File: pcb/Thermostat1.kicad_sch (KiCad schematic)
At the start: 50 parts, among them J1 Screw_Terminal_01x04, J2 Conn_01x04_Female, K1 HK19F-DC_12-SHG, K2 HK19F-DC_12-SHG, Q1 SI2310B, Q2 SI2310B, SW1 SW_Push, SW2 SW_Push, SW3 SW_Push, SW4 SW_Push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

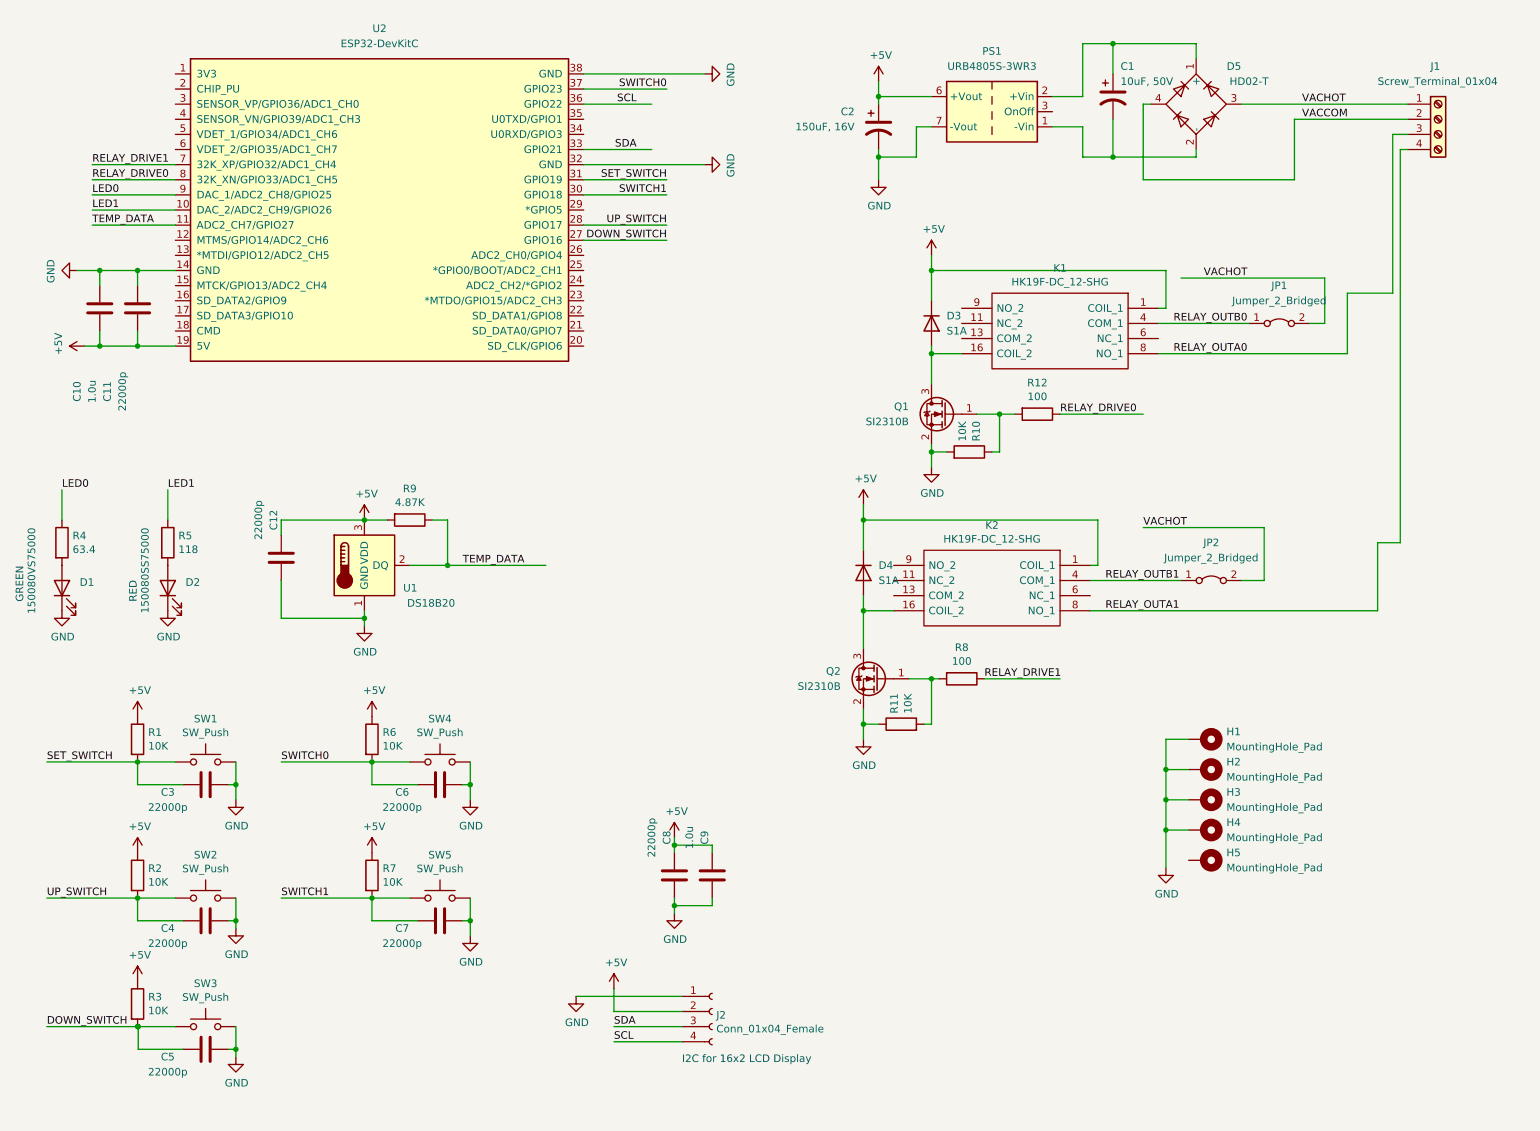
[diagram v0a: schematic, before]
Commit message: Fixed a couple issues on schematic and layout - swapped power supplies on external components and pullups from 5V to 3.3V, moved input connector so it's further from the edge of the box, increased spacing on thermometer leads to accomodate available parts and added an FCCH logo.
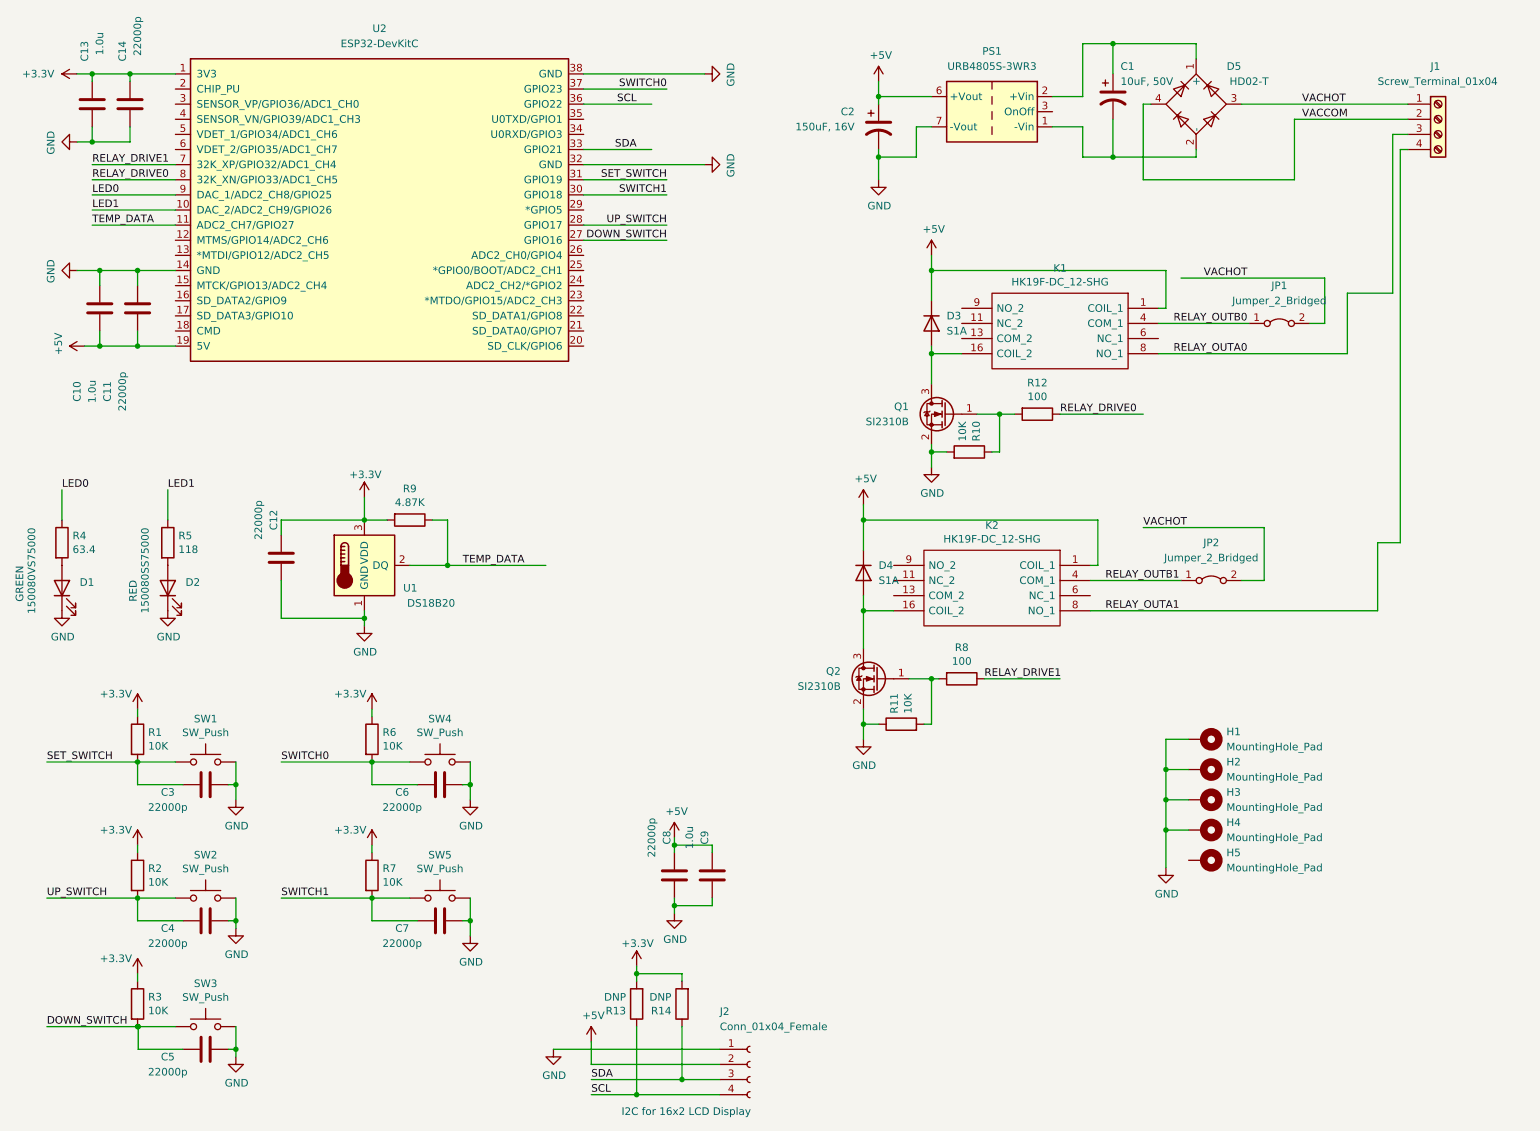
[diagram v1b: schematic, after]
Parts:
- added C13: 1.0u, Capacitor_SMD:C_0805_2012Metric_Pad1.18x1.45mm_HandSolder, symbol Device:C
- added C14: 22000p, Capacitor_SMD:C_0603_1608Metric_Pad1.08x0.95mm_HandSolder, symbol Device:C
- added R13, R14: DNP, Resistor_SMD:R_0603_1608Metric_Pad0.98x0.95mm_HandSolder, symbol Device:R
- U1: footprint Package_TO_SOT_THT:TO-92_Inline -> Package_TO_SOT_THT:TO-92_Inline_Wide
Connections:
- net +5V: no longer C12.1, R1.1, R2.1, R3.1, R6.1, R7.1, R9.2, U1.3 (VDD)
- net GND: now also C13.2, C14.2
- net SCL: now also R13.1
- net SDA: now also R14.1
- net +3.3V: now reaches U2.1 (3V3)
- net +3.3V: now also C12.1, R1.1, R2.1, R3.1, R6.1, R7.1, R9.2, U1.3 (VDD), C13.1, C14.1, R13.2, R14.2
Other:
- moved on the sheet: J2

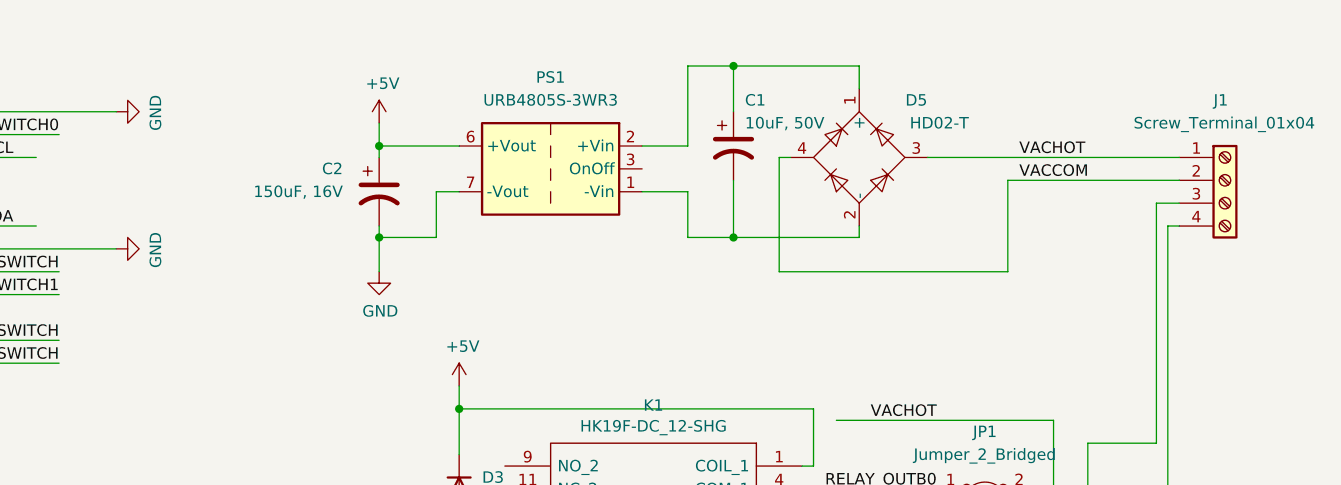
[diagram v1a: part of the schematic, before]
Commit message: A few more fixes for Rev 0.3 - more options for power input caps as well as some sense resistors, also remade gerber files.
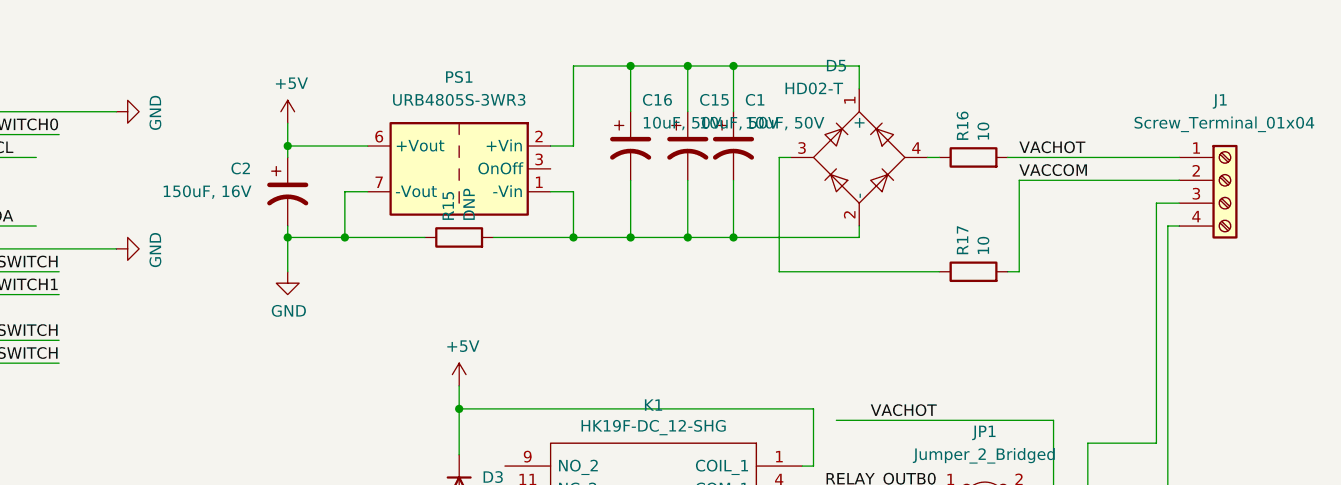
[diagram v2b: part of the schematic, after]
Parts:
- added C15: 10uF, 50V, Capacitor_THT:CP_Radial_D5.0mm_P2.00mm, symbol Device:C_Polarized_US
- added C16: 10uF, 50V, Capacitor_THT:CP_Radial_D8.0mm_P5.00mm, symbol Device:C_Polarized_US
- added R15: DNP, Resistor_SMD:R_1206_3216Metric_Pad1.30x1.75mm_HandSolder, symbol Device:R
- added R16, R17: 10, Resistor_SMD:R_1206_3216Metric_Pad1.30x1.75mm_HandSolder, symbol Device:R
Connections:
- net GND: now also R15.1
- net VACCOM: now also R17.2; no longer D5.4
- net VACHOT: now also R16.2; no longer D5.3
- net at C1.1, D5.1 (+), PS1.2 (+Vin): now also C15.1, C16.1
- net at C1.2, D5.2 (-), PS1.1 (-Vin): now also C15.2, C16.2, R15.2
- new net: D5.3, R17.1
- new net: D5.4, R16.1
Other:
- moved on the sheet: C2, D5, PS1
